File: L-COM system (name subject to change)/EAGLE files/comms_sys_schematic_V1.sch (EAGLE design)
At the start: 49 parts, among them U1 R-78C5.0-1.0, U2 TLV75733PDBVR, X1 SMA-142-0701-801/806, Y1 ECS-TXO-2016-33-120-TR

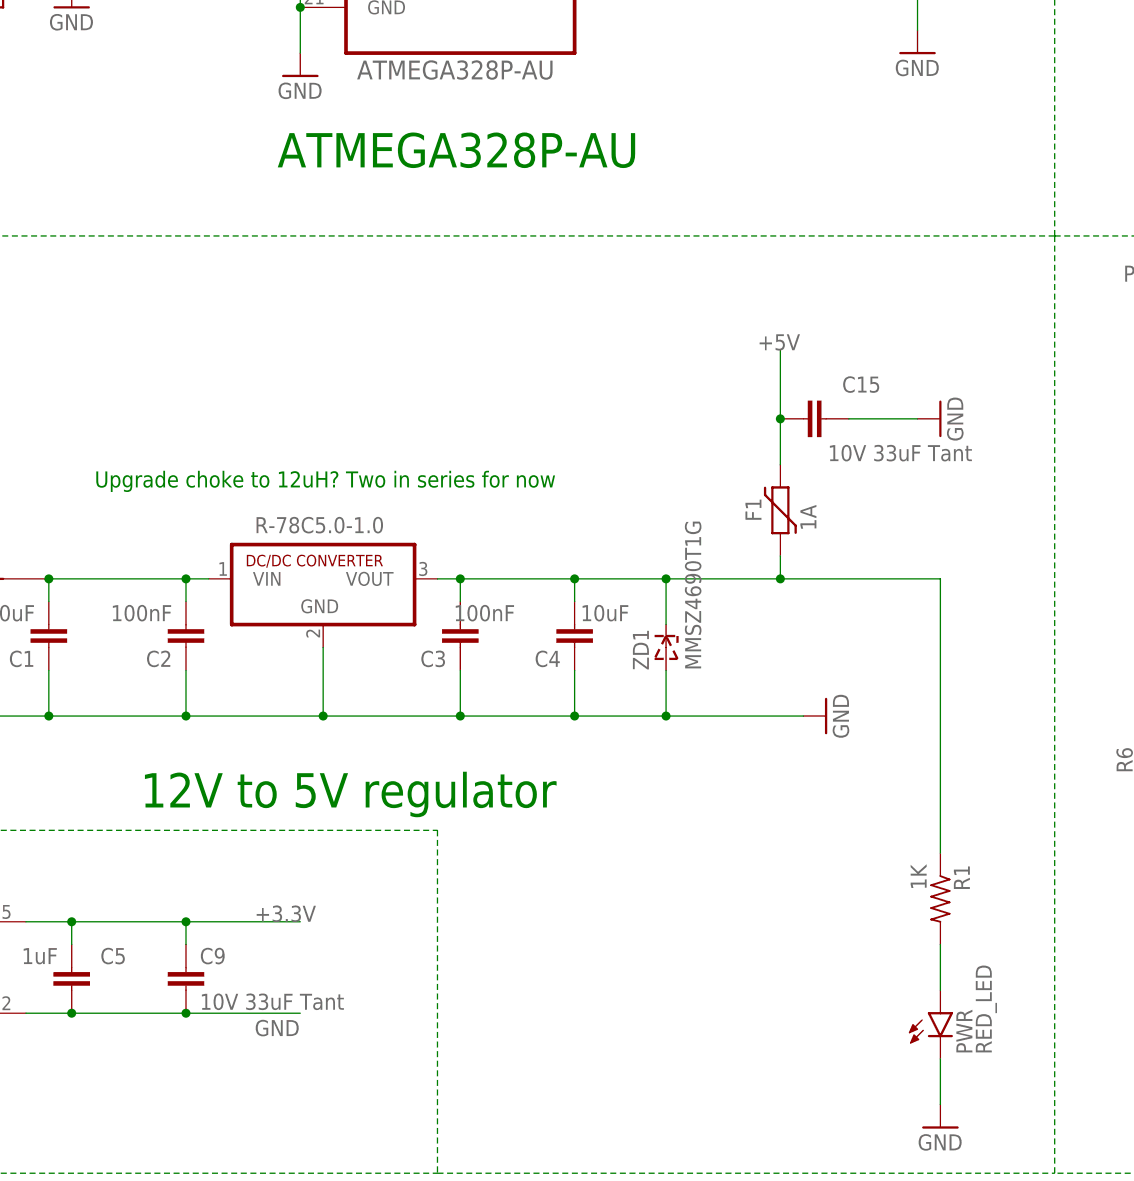
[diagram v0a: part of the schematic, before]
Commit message: Replaced footprints for tantalum capacitors
Swapped out the tantalum capacitor's footprints for a slightly different one. Includes polarity marking on silkscreen.
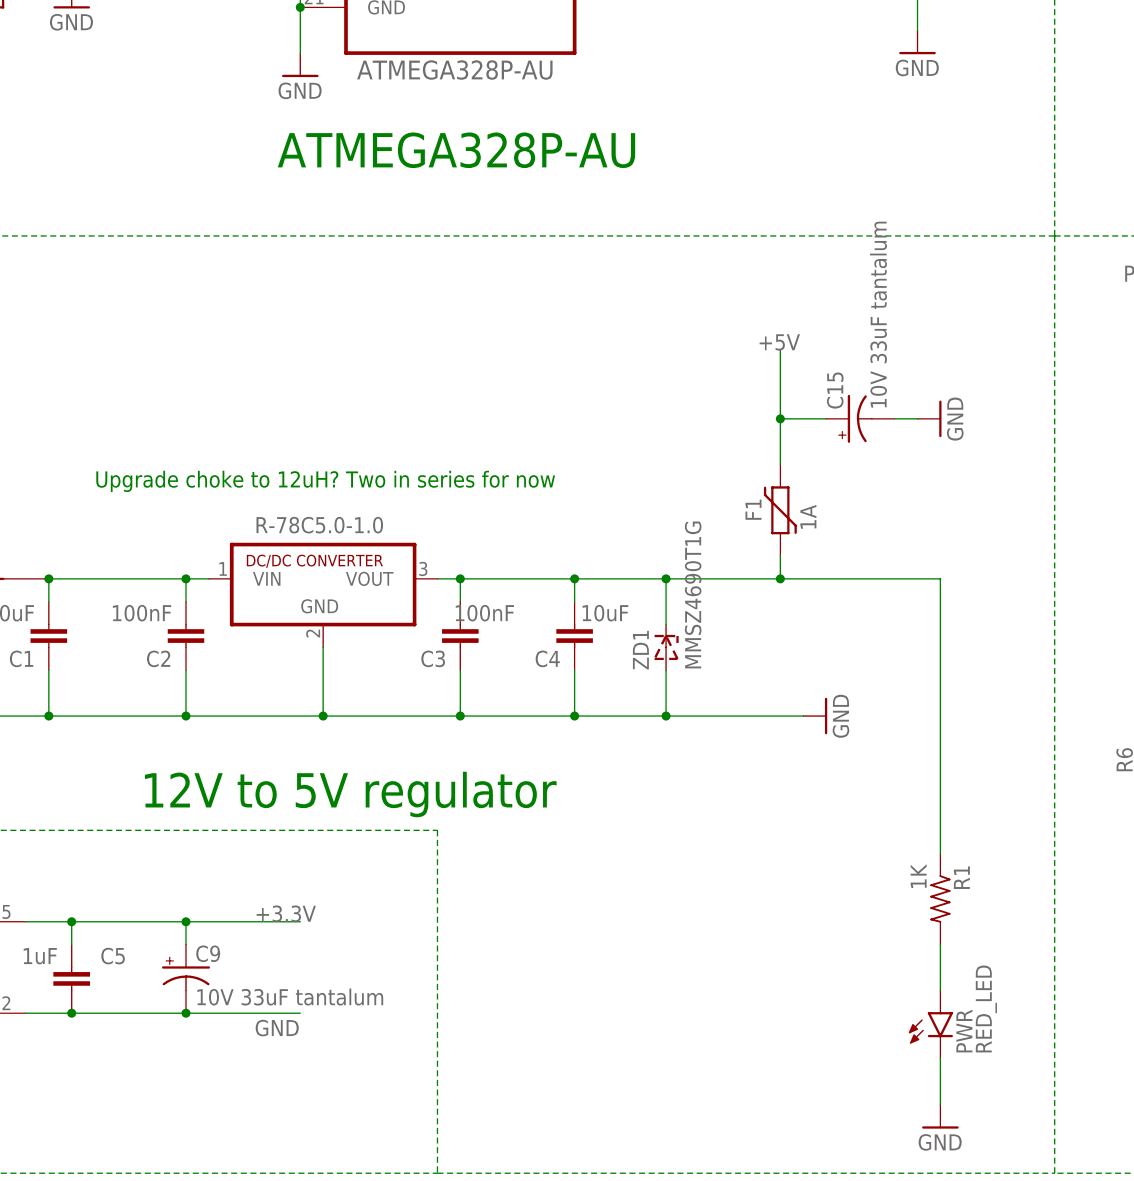
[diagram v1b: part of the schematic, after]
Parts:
- C15, C9: value 10V 33uF Tant -> 10V 33uF tantalum; device rcl:C-EUC1206 -> rcl:CPOL-USCT3216
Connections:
- net +3.3V: now also C9.+; no longer C9.1
- net +5V: now also C15.+; no longer C15.1
- net GND: now also C15.-, C9.-; no longer C15.2, C9.2
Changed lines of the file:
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@@
 <part name="C17" library="rcl" library_urn="urn:adsk.eagle:library:334" deviceset="C-EU" device="C0805" package3d_urn="urn:adsk.eagle:package:23617/2" value="100nF"/>
 <part name="GND18" library="supply1" library_urn="urn:adsk.eagle:library:371" deviceset="GND" device=""/>
-<part name="C9" library="rcl" library_urn="urn:adsk.eagle:library:334" deviceset="C-EU" device="C1206" package3d_urn="urn:adsk.eagle:package:23618/2" value="10V 33uF Tant"/>
-<part name="C15" library="rcl" library_urn="urn:adsk.eagle:library:334" deviceset="C-EU" device="C1206" package3d_urn="urn:adsk.eagle:package:23618/2" value="10V 33uF Tant"/>
 <part name="GND19" library="supply1" library_urn="urn:adsk.eagle:library:371" deviceset="GND" device=""/>
 <part name="X1" library="con-coax" library_urn="urn:adsk.eagle:library:133" deviceset="SMA-" device="142-0701-801/806" package3d_urn="urn:adsk.eagle:package:6214/1"/>
 <part name="SW1" library="Wurth_Elektronik_Electromechanic_Switch_rev16c" deviceset="430152043826" device=""/>
 <part name="R4" library="1624345-1" deviceset="1624345-1" device=""/>
+<part name="C9" library="rcl" library_urn="urn:adsk.eagle:library:334" deviceset="CPOL-US" device="CT3216" package3d_urn="urn:adsk.eagle:package:23327/2" value="10V 33uF tantalum"/>
+<part name="C15" library="rcl" library_urn="urn:adsk.eagle:library:334" deviceset="CPOL-US" device="CT3216" package3d_urn="urn:adsk.eagle:package:23327/2" value="10V 33uF tantalum"/>
 </parts>
 <sheets>
@@
 <attribute name="VALUE" x="-7.62" y="68.58" size="1.778" layer="96"/>
 </instance>
-<instance part="C9" gate="G$1" x="-66.04" y="-58.42" smashed="yes">
-<attribute name="NAME" x="-64.516" y="-58.039" size="1.778" layer="95"/>
-<attribute name="VALUE" x="-64.516" y="-63.119" size="1.778" layer="96"/>
-</instance>
-<instance part="C15" gate="G$1" x="2.54" y="2.54" smashed="yes" rot="R90">
-<attribute name="NAME" x="11.176" y="7.239" size="1.778" layer="95" rot="R180"/>
-<attribute name="VALUE" x="21.336" y="-0.381" size="1.778" layer="96" rot="R180"/>
-</instance>
 <instance part="GND19" gate="1" x="17.78" y="2.54" smashed="yes" rot="R90">
 <attribute name="VALUE" x="20.32" y="0" size="1.778" layer="96" rot="R90"/>
@@
 <attribute name="NAME" x="-103.89721875" y="163.07548125" size="2.543740625" layer="95"/>
 <attribute name="VALUE" x="-111.76605" y="152.3919" size="2.54201875" layer="96"/>
+</instance>
+<instance part="C9" gate="G$1" x="-66.04" y="-58.42" smashed="yes">
+<attribute name="NAME" x="-65.024" y="-57.785" size="1.778" layer="95"/>
+<attribute name="VALUE" x="-65.024" y="-62.611" size="1.778" layer="96"/>
+</instance>
+<instance part="C15" gate="G$1" x="7.62" y="2.54" smashed="yes" rot="R90">
+<attribute name="NAME" x="6.985" y="3.556" size="1.778" layer="95" rot="R90"/>
+<attribute name="VALUE" x="11.811" y="3.556" size="1.778" layer="96" rot="R90"/>
 </instance>
 </instances>
@@
 <wire x1="-78.74" y1="-63.5" x2="-66.04" y2="-63.5" width="0.1524" layer="91"/>
 <junction x="-78.74" y="-63.5"/>
-<pinref part="C9" gate="G$1" pin="2"/>
 <wire x1="-66.04" y1="-63.5" x2="-53.34" y2="-63.5" width="0.1524" layer="91"/>
 <junction x="-66.04" y="-63.5"/>
+<pinref part="C9" gate="G$1" pin="-"/>
 </segment>
 <segment>
@@
 </segment>
 <segment>
-<pinref part="C15" gate="G$1" pin="2"/>
-<wire x1="7.62" y1="2.54" x2="15.24" y2="2.54" width="0.1524" layer="91"/>
+<wire x1="12.7" y1="2.54" x2="15.24" y2="2.54" width="0.1524" layer="91"/>
 <pinref part="GND19" gate="1" pin="GND"/>
+<pinref part="C15" gate="G$1" pin="-"/>
 </segment>
 <segment>
@@
 <wire x1="0" y1="-2.54" x2="0" y2="2.54" width="0.1524" layer="91"/>
 <label x="-2.54" y="10.16" size="1.778" layer="95"/>
-<pinref part="C15" gate="G$1" pin="1"/>
 <wire x1="0" y1="2.54" x2="0" y2="10.16" width="0.1524" layer="91"/>
 <junction x="0" y="2.54"/>
+<wire x1="0" y1="2.54" x2="5.08" y2="2.54" width="0.1524" layer="91"/>
+<pinref part="C15" gate="G$1" pin="+"/>
 </segment>
 <segment>
@@
 <label x="-58.42" y="-53.34" size="1.778" layer="95"/>
 <junction x="-78.74" y="-53.34"/>
-<pinref part="C9" gate="G$1" pin="1"/>
 <wire x1="-66.04" y1="-53.34" x2="-53.34" y2="-53.34" width="0.1524" layer="91"/>
 <wire x1="-66.04" y1="-55.88" x2="-66.04" y2="-53.34" width="0.1524" layer="91"/>
 <junction x="-66.04" y="-53.34"/>
-</segment>
-<segment>
+<pinref part="C9" gate="G$1" pin="+"/>
+</segment>
+<segment>
